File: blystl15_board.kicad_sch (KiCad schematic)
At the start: 28 parts, among them J1 SSD1306, J2 Conn_01x02, J3 USB_C_Receptacle_USB2.0_16P, J4 BNO085, P2 ARM JTAG/SWD, SW1 SW_SPDT, SW2 SW_Push, SW3 SW_Push, SW4 SW_Push, U1 MCP73831-2-OT, U2 AP2112K-3.3

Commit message: Schematic Draft
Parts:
- removed C4: 4.7µF, symbol Device:C
- removed C5, C6: 1µF, symbol Device:C
- removed D1: LED, symbol Device:LED
- removed J2: Conn_01x02, symbol Connector_Generic:Conn_01x02
- removed J3: USB_C_Receptacle_USB2.0_16P, symbol Connector:USB_C_Receptacle_USB2.0_16P
- removed P2: ARM JTAG/SWD, 1_I-SYST_inc:CON10_2X5_DUK_FTSH_SAI-M, symbol I_Syst_inc:FTSH-105-01-L-DV-K-TR
- removed R3, R4: 5.1kΩ, symbol Device:R
- removed R5: 2kΩ, symbol Device:R
- removed R6: 1kΩ, symbol Device:R
- removed SW1: SW_SPDT, symbol Switch:SW_SPDT
- removed U1: MCP73831-2-OT, Package_TO_SOT_SMD:SOT-23-5, symbol Battery_Management:MCP73831-2-OT
- removed U2: AP2112K-3.3, Package_TO_SOT_SMD:SOT-23-5, symbol Regulator_Linear:AP2112K-3.3
- added J2: Conn_01x03, symbol Connector_Generic:Conn_01x03
- added J3: DOCK_PADS, symbol Connector_Generic:Conn_01x06
- added L1: 1.0µH, Inductor_SMD:L_0805_2012Metric, symbol Device:L
- added U1: NPM1304-QEAA-R7, 1_I-SYST_inc:QFN50P500X500X90-33N, symbol I_Syst_inc:NPM1304-QEAA-R7
- added U2: MAX30102EFD+T, 1_I-SYST_inc:21-1048_F143A5&plus_1_MXM-L, symbol I_Syst_inc:MAX30102EFD+T
- added U3: MAX30208CLB+T, 1_I-SYST_inc:21-100265_MXM, symbol I_Syst_inc:MAX30208CLB+T
- C1: footprint (none) -> Capacitor_SMD:C_0603_1608Metric
- C2: footprint (none) -> Capacitor_SMD:C_0402_1005Metric
- C3: value 4.7µF -> 10µF; footprint (none) -> Capacitor_SMD:C_0603_1608Metric
- C4: renamed from C7; footprint (none) -> Capacitor_SMD:C_0402_1005Metric
- C5: renamed from C8; footprint (none) -> Capacitor_SMD:C_0402_1005Metric
- C6: renamed from C9; footprint (none) -> Capacitor_SMD:C_0402_1005Metric
- R1, R2: footprint (none) -> Resistor_SMD:R_0402_1005Metric
- SW2, SW3, SW4: footprint (none) -> Button_Switch_SMD:SW_Push_1P1T_NO_CK_KSC7xxJ
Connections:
- net P1.11 is gone; now on net P1.11  AIN4: J4.4 (Pin_4)
- net P1.12 is gone; now on net P1.12  AIN5: J4.3 (Pin_3)
- net GND: now also J4.1 (Pin_1), J4.2 (Pin_2), J4.6 (Pin_6), J2.2 (Pin_2), J3.2 (Pin_2), U1.2 (PVSS1), U1.33 (AVSS), U1.6 (PVSS2), U2.12 (GND), U2.4 (PGND), U3.4 (GND), U3.5 (GND), U3.6 (GND)
- net P1.09: now also U1.13 (SDA), U2.3 (SDA), U3.8 (SDA)
- net P1.10: now also U1.14 (SCL), U2.2 (SCL), U3.9 (SCL)
- net P1.15: now also U2.13 (*INT)
- net P2.06: now also U3.7 (GPIO1)
- net P2.07: now also U1.7 (GPIO0)
- net P2.09: now also U1.15 (SHPHLD)
- net P2.10: now also U3.10 (GPIO0)
- net SWDCLK: now also J3.4 (Pin_4)
- net SWDIO: now also J3.3 (Pin_3)
- net VBAT: now also J2.1 (Pin_1), U1.19 (VBAT), U2.10 (VLED+), U2.9 (VLED+)
- net VBUS: now also J3.1 (Pin_1), U1.21 (VBUS); no longer C3.1
- net VDD: now also C3.1, J4.5 (Pin_5), J3.6 (Pin_6), L1.1, U1.1 (VOUT1), U1.12 (VDDIO), U2.11 (VDD), U3.1 (VDD), U3.2 (VDD), U3.3 (VDD)
- net nRESET: now also J3.5 (Pin_5)
- new net: U1.20 (VSYS), U1.4 (PVDD)
- new net: L1.2, U1.3 (SW1)
- new net NTC: J2.3 (Pin_3), U1.18 (NTC)
- no-connect marks 6 -> 43
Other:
- note added: "Heart Rate Sensor"
- note added: "LiPo Battery (3.7V 400mAh)"
- note added: "Power Management IC"
- note added: "SWCLK"
- note added: "Temperature Sensor"
- note added: "nRF54L15 BLE module"
- note removed: "Battery"
- note removed: "Cortex Debug Connector"
- moved on the sheet: C1, C4, C5, C6, J1, J4, R1, R2, SW2, SW3, SW4

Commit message: All footprints imported in PCB editor
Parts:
- J1: footprint (none) -> Connector_PinSocket_2.54mm:PinSocket_1x04_P2.54mm_Vertical
- J2: footprint (none) -> Connector_JST:JST_PH_S3B-PH-SM4-TB_1x03-1MP_P2.00mm_Horizontal
- J3: footprint (none) -> 1_I-SYST_inc:Dock_Pads_6Pin
- J4: footprint (none) -> Connector_PinSocket_2.54mm:PinSocket_1x10_P2.54mm_Vertical
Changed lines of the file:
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@@
 			)
 		)
-		(property "Footprint" ""
+		(property "Footprint" "1_I-SYST_inc:Dock_Pads_6Pin"
 			(at 242.57 62.23 0)
 			(effects
@@
 			)
 		)
-		(property "Footprint" ""
+		(property "Footprint" "Connector_JST:JST_PH_S3B-PH-SM4-TB_1x03-1MP_P2.00mm_Horizontal"
 			(at 242.57 36.83 0)
 			(effects
@@
 			)
 		)
-		(property "Footprint" ""
+		(property "Footprint" "Connector_PinSocket_2.54mm:PinSocket_1x04_P2.54mm_Vertical"
 			(at 242.57 104.14 0)
 			(effects
@@
 			)
 		)
-		(property "Footprint" ""
+		(property "Footprint" "Connector_PinSocket_2.54mm:PinSocket_1x10_P2.54mm_Vertical"
 			(at 168.91 139.7 0)
 			(effects
@@
 			)
 		)
-		(property "Datasheet" "~"
+		(property "Datasheet" "https://www.ceva-ip.com/wp-content/uploads/BNO080_085-Datasheet.pdf"
 			(at 168.91 139.7 0)
 			(effects

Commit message: Created custom footprints to match dimension of external boards
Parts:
- J1: footprint Connector_PinSocket_2.54mm:PinSocket_1x04_P2.54mm_Vertical -> 1_I-SYST_inc:OLED_1.3in_I2C
- J4: footprint Connector_PinSocket_2.54mm:PinSocket_1x10_P2.54mm_Vertical -> 1_I-SYST_inc:BNO085_Module
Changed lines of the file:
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@@
 			)
 		)
-		(property "Footprint" "Connector_PinSocket_2.54mm:PinSocket_1x04_P2.54mm_Vertical"
+		(property "Footprint" "1_I-SYST_inc:OLED_1.3in_I2C"
 			(at 242.57 104.14 0)
 			(effects
@@
 			)
 		)
-		(property "Footprint" "Connector_PinSocket_2.54mm:PinSocket_1x10_P2.54mm_Vertical"
+		(property "Footprint" "1_I-SYST_inc:BNO085_Module"
 			(at 168.91 139.7 0)
 			(effects

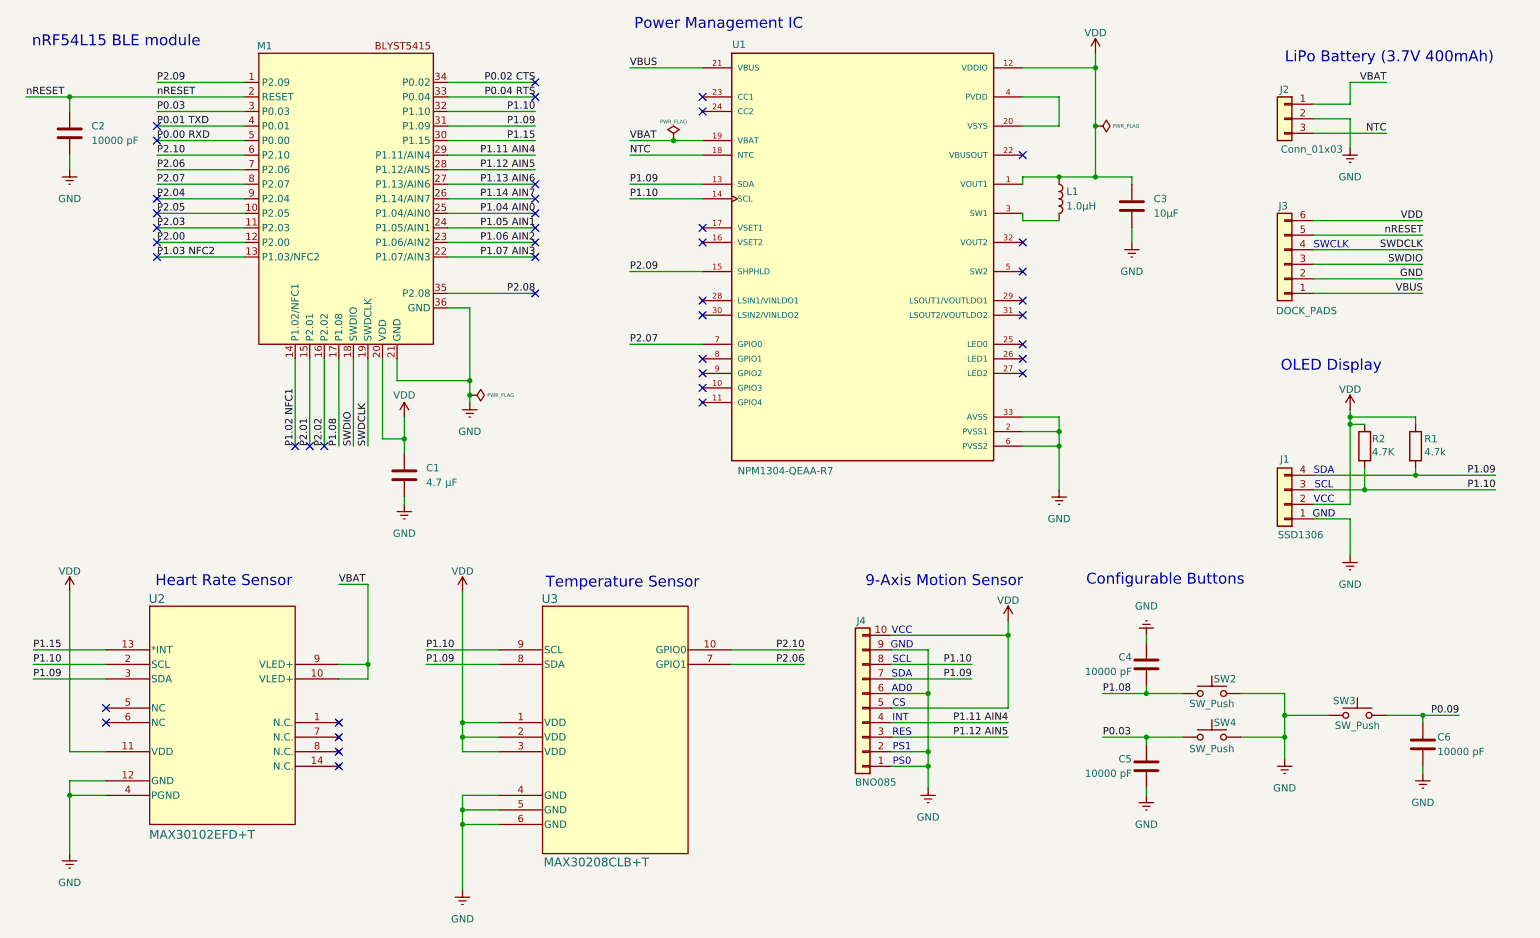
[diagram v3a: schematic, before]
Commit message: Reorganization into multiple sheet and addition of BMP384, W25Q80DVSSIG and OPT3001DNPRQ1
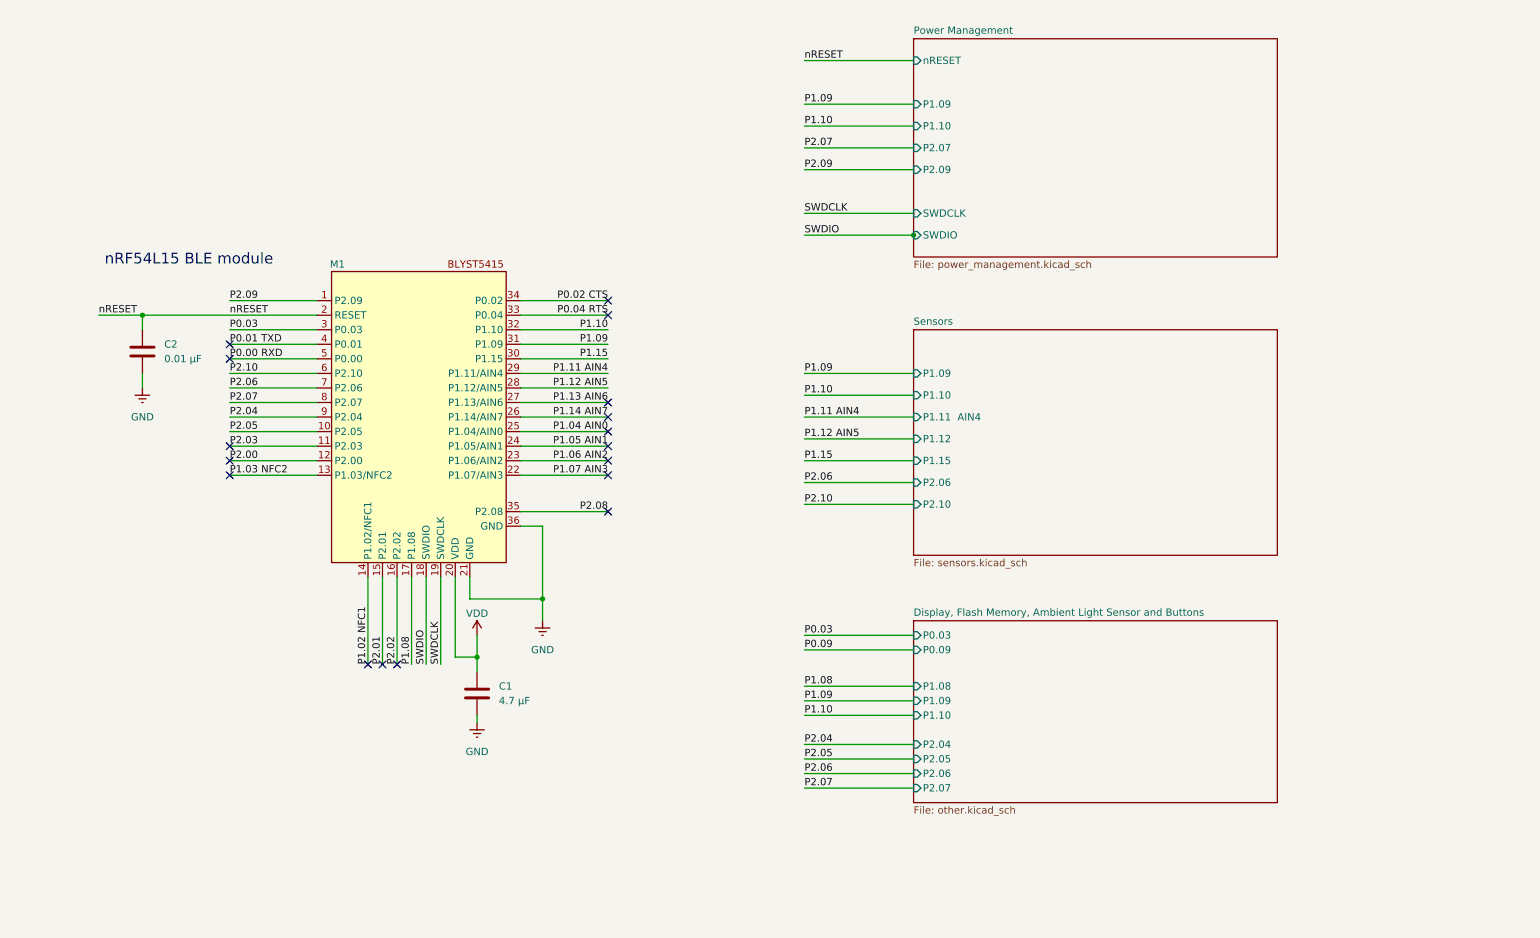
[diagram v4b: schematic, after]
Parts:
- removed C3: 10µF, Capacitor_SMD:C_0603_1608Metric, symbol Device:C
- removed C4, C5, C6: 10000 pF, Capacitor_SMD:C_0402_1005Metric, symbol Device:C
- removed J1: SSD1306, 1_I-SYST_inc:OLED_1.3in_I2C, symbol Connector_Generic:Conn_01x04
- removed J2: Conn_01x03, Connector_JST:JST_PH_S3B-PH-SM4-TB_1x03-1MP_P2.00mm_Horizontal, symbol Connector_Generic:Conn_01x03
- removed J3: DOCK_PADS, 1_I-SYST_inc:Dock_Pads_6Pin, symbol Connector_Generic:Conn_01x06
- removed J4: BNO085, 1_I-SYST_inc:BNO085_Module, symbol Connector_Generic:Conn_01x10
- removed L1: 1.0µH, Inductor_SMD:L_0805_2012Metric, symbol Device:L
- removed R1: 4.7k, Resistor_SMD:R_0402_1005Metric, symbol Device:R
- removed R2: 4.7K, Resistor_SMD:R_0402_1005Metric, symbol Device:R
- removed SW2, SW3, SW4: SW_Push, Button_Switch_SMD:SW_Push_1P1T_NO_CK_KSC7xxJ, symbol Switch:SW_Push
- removed U1: NPM1304-QEAA-R7, 1_I-SYST_inc:QFN50P500X500X90-33N, symbol I_Syst_inc:NPM1304-QEAA-R7
- removed U2: MAX30102EFD+T, 1_I-SYST_inc:21-1048_F143A5&plus_1_MXM-L, symbol I_Syst_inc:MAX30102EFD+T
- removed U3: MAX30208CLB+T, 1_I-SYST_inc:21-100265_MXM, symbol I_Syst_inc:MAX30208CLB+T
- C1: Price (none) -> 0.1
- C2: value 10000 pF -> 0.01 μF; Price (none) -> 0.1
- M1: Price (none) -> 4.03
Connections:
- no-connect marks 43 -> 17
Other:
- added sheet Display, Flash Memory, Ambient Light Sensor and Buttons (other.kicad_sch)
- added sheet Power Management (power_management.kicad_sch)
- added sheet Sensors (sensors.kicad_sch)
- note removed: "9-Axis Motion Sensor"
- note removed: "AD0"
- note removed: "CS"
- note removed: "Configurable Buttons"
- note removed: "GND"
- note removed: "Heart Rate Sensor"
- note removed: "INT"
- note removed: "LiPo Battery (3.7V 400mAh)"
- note removed: "OLED Display"
- note removed: "PS0"
- note removed: "PS1"
- note removed: "Power Management IC"
- note removed: "RES"
- note removed: "SCL"
- note removed: "SDA"
- note removed: "SWCLK"
- note removed: "Temperature Sensor"
- note removed: "VCC"
- title: BLYSTL15 -> Smart Watch L15
- moved on the sheet: C1, C2, M1

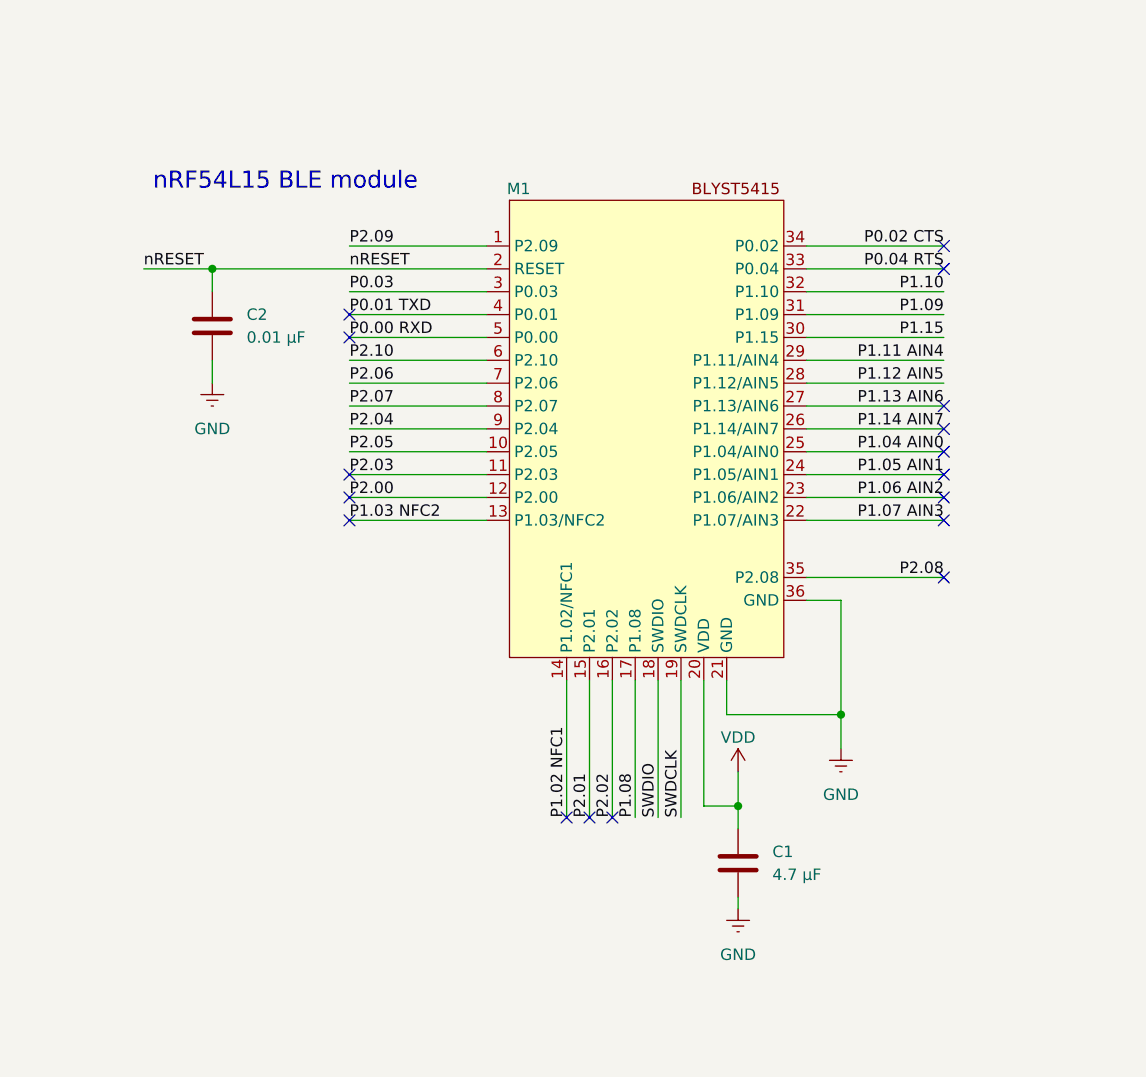
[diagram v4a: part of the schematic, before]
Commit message: New Symbol for BlystL15
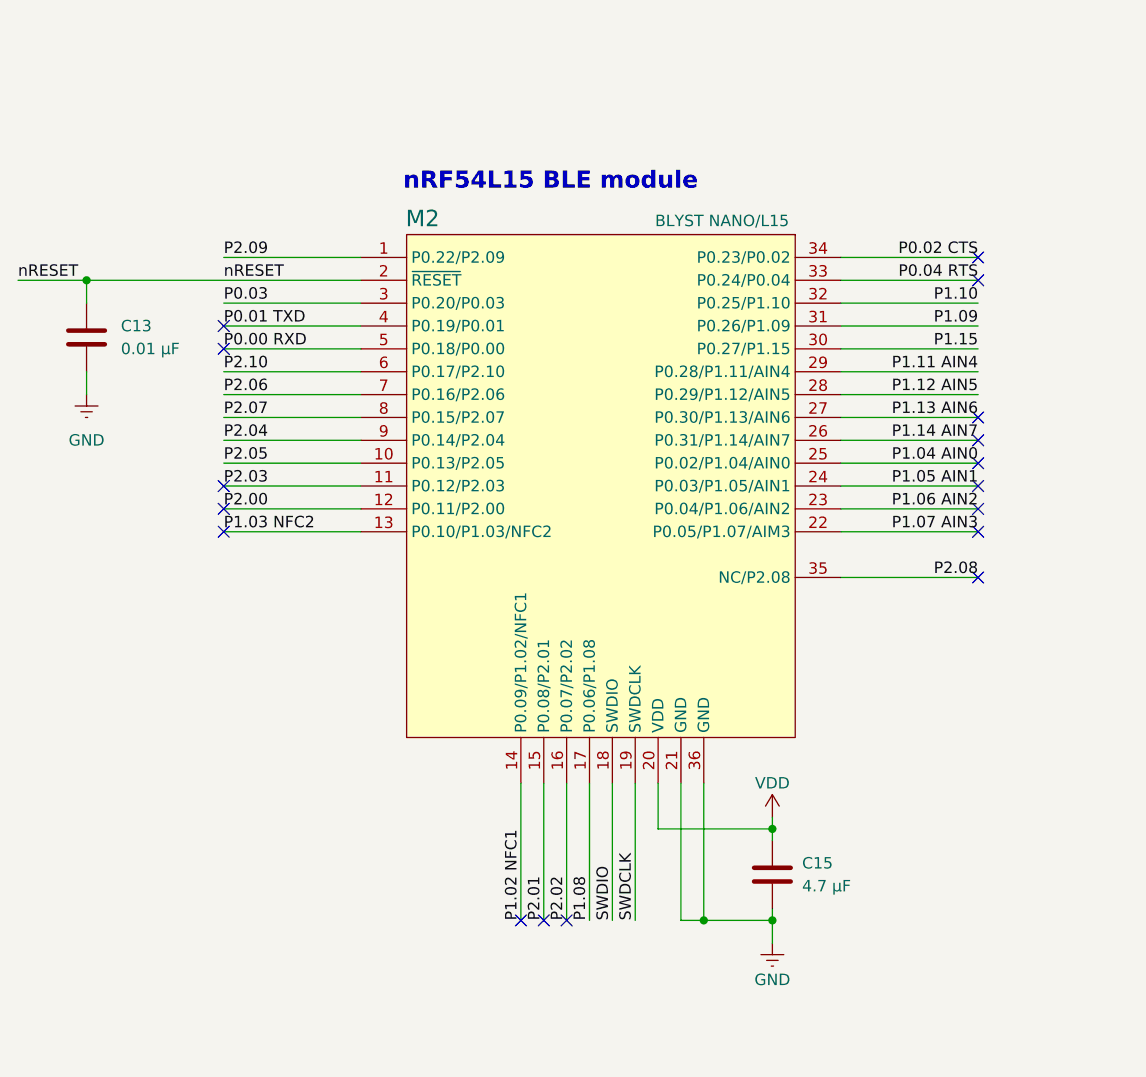
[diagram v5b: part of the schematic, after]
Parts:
- removed C1: 4.7 μF, Capacitor_SMD:C_0603_1608Metric, symbol Device:C
- removed C2: 0.01 μF, Capacitor_SMD:C_0402_1005Metric, symbol Device:C
- removed M1: ~, 1_I-SYST_inc:BLYSTL15, symbol I_Syst_inc:BLYSTL15
- added C13: 0.01 μF, Capacitor_SMD:C_0402_1005Metric, symbol Device:C
- added C15: 4.7 μF, Capacitor_SMD:C_0603_1608Metric, symbol Device:C
- added M2: BLYST NANO/L15, BLYSTL15, symbol From_Altium:BLYSTNANO_L15
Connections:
- net GND: now also C13.2, C15.2, M2.21 (GND), M2.36 (GND)
- net P0.00  RXD: now also M2.5 (P0.18/P0.00)
- net P0.01  TXD: now also M2.4 (P0.19/P0.01)
- net P0.02  CTS: now also M2.34 (P0.23/P0.02)
- net P0.03: now also M2.3 (P0.20/P0.03)
- net P0.04  RTS: now also M2.33 (P0.24/P0.04)
- net P1.02  NFC1: now also M2.14 (P0.09/P1.02/NFC1)
- net P1.03  NFC2: now also M2.13 (P0.10/P1.03/NFC2)
- net P1.04  AIN0: now also M2.25 (P0.02/P1.04/AIN0)
- net P1.05  AIN1: now also M2.24 (P0.03/P1.05/AIN1)
- net P1.06  AIN2: now also M2.23 (P0.04/P1.06/AIN2)
- net P1.07  AIN3: now also M2.22 (P0.05/P1.07/AIM3)
- net P1.08: now also M2.17 (P0.06/P1.08)
- net P1.09: now also M2.31 (P0.26/P1.09)
- net P1.10: now also M2.32 (P0.25/P1.10)
- net P1.11  AIN4: now also M2.29 (P0.28/P1.11/AIN4)
- net P1.12  AIN5: now also M2.28 (P0.29/P1.12/AIN5)
- net P1.13  AIN6: now also M2.27 (P0.30/P1.13/AIN6)
- net P1.14  AIN7: now also M2.26 (P0.31/P1.14/AIN7)
- net P1.15: now also M2.30 (P0.27/P1.15)
- net P2.00: now also M2.12 (P0.11/P2.00)
- net P2.01: now also M2.15 (P0.08/P2.01)
- net P2.02: now also M2.16 (P0.07/P2.02)
- net P2.03: now also M2.11 (P0.12/P2.03)
- net P2.04: now also M2.9 (P0.14/P2.04)
- net P2.05: now also M2.10 (P0.13/P2.05)
- net P2.06: now also M2.7 (P0.16/P2.06)
- net P2.07: now also M2.8 (P0.15/P2.07)
- net P2.08: now also M2.35 (NC/P2.08)
- net P2.09: now also M2.1 (P0.22/P2.09)
- net P2.10: now also M2.6 (P0.17/P2.10)
- net SWDCLK: now also M2.19 (SWDCLK)
- net SWDIO: now also M2.18 (SWDIO)
- net VDD: now also C15.1, M2.20 (VDD)
- net nRESET: now also C13.1, M2.2 (~{RESET})

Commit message: Organized components in pcb layout editor
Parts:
- removed C13: 0.01 μF, Capacitor_SMD:C_0402_1005Metric, symbol Device:C
- removed C15: 4.7 μF, Capacitor_SMD:C_0603_1608Metric, symbol Device:C
- removed M2: BLYST NANO/L15, BLYSTL15, symbol From_Altium:BLYSTNANO_L15
- added C1: 4.7 μF, Capacitor_SMD:C_0603_1608Metric, symbol Device:C
- added C9: 0.01 μF, Capacitor_SMD:C_0402_1005Metric, symbol Device:C
- added M1: BLYST NANO/L15, 1_I_Syst.inc:BLYSTL15, symbol From_Altium:BLYSTNANO_L15
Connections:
- net GND: now also C1.2, C9.2, M1.21 (GND), M1.36 (GND)
- net P0.00  RXD: now also M1.5 (P0.18/P0.00)
- net P0.01  TXD: now also M1.4 (P0.19/P0.01)
- net P0.02  CTS: now also M1.34 (P0.23/P0.02)
- net P0.03: now also M1.3 (P0.20/P0.03)
- net P0.04  RTS: now also M1.33 (P0.24/P0.04)
- net P1.02  NFC1: now also M1.14 (P0.09/P1.02/NFC1)
- net P1.03  NFC2: now also M1.13 (P0.10/P1.03/NFC2)
- net P1.04  AIN0: now also M1.25 (P0.02/P1.04/AIN0)
- net P1.05  AIN1: now also M1.24 (P0.03/P1.05/AIN1)
- net P1.06  AIN2: now also M1.23 (P0.04/P1.06/AIN2)
- net P1.07  AIN3: now also M1.22 (P0.05/P1.07/AIM3)
- net P1.08: now also M1.17 (P0.06/P1.08)
- net P1.09: now also M1.31 (P0.26/P1.09)
- net P1.10: now also M1.32 (P0.25/P1.10)
- net P1.11  AIN4: now also M1.29 (P0.28/P1.11/AIN4)
- net P1.12  AIN5: now also M1.28 (P0.29/P1.12/AIN5)
- net P1.13  AIN6: now also M1.27 (P0.30/P1.13/AIN6)
- net P1.14  AIN7: now also M1.26 (P0.31/P1.14/AIN7)
- net P1.15: now also M1.30 (P0.27/P1.15)
- net P2.00: now also M1.12 (P0.11/P2.00)
- net P2.01: now also M1.15 (P0.08/P2.01)
- net P2.02: now also M1.16 (P0.07/P2.02)
- net P2.03: now also M1.11 (P0.12/P2.03)
- net P2.04: now also M1.9 (P0.14/P2.04)
- net P2.05: now also M1.10 (P0.13/P2.05)
- net P2.06: now also M1.7 (P0.16/P2.06)
- net P2.07: now also M1.8 (P0.15/P2.07)
- net P2.08: now also M1.35 (NC/P2.08)
- net P2.09: now also M1.1 (P0.22/P2.09)
- net P2.10: now also M1.6 (P0.17/P2.10)
- net SWDCLK: now also M1.19 (SWDCLK)
- net SWDIO: now also M1.18 (SWDIO)
- net VDD: now also C1.1, M1.20 (VDD)
- net nRESET: now also C9.1, M1.2 (~{RESET})
- no-connect marks 17 -> 16
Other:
- sheet Display, Flash Memory, Ambient Light Sensor and Buttons ports: added P2.00; removed P0.09
- sheet Sensors ports: added P2.03; removed P1.12, P2.06
